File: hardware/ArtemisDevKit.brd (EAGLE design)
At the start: 94 x 38.1 mm, 231 parts, among them J1 USB, J10 SMD, J11 SMD, J12 PTH, J14 PTH, J2 CORTEX_JTAG_DEBUG_MINIMUM_PTH, J22 PTH, J23 PTH, J24 PTH, J25 PTH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

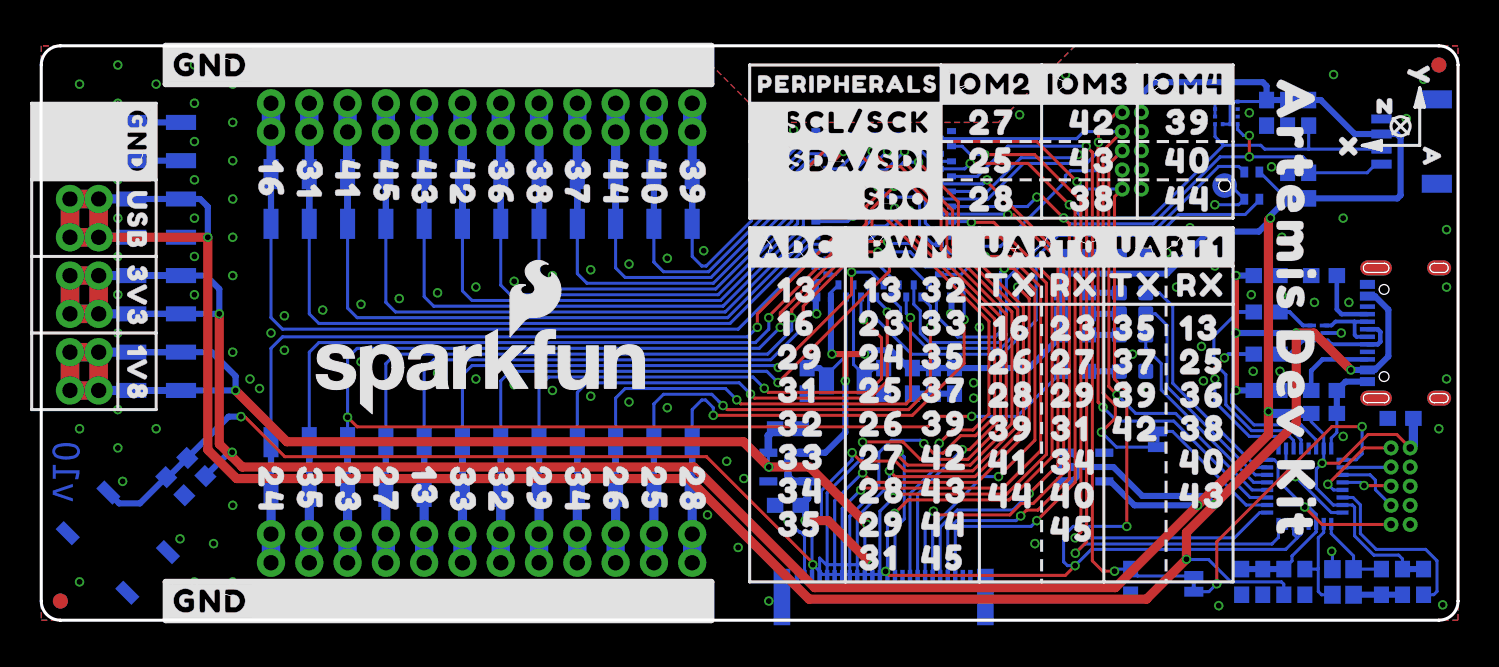
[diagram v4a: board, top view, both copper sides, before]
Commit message: add test points for interface JTAG
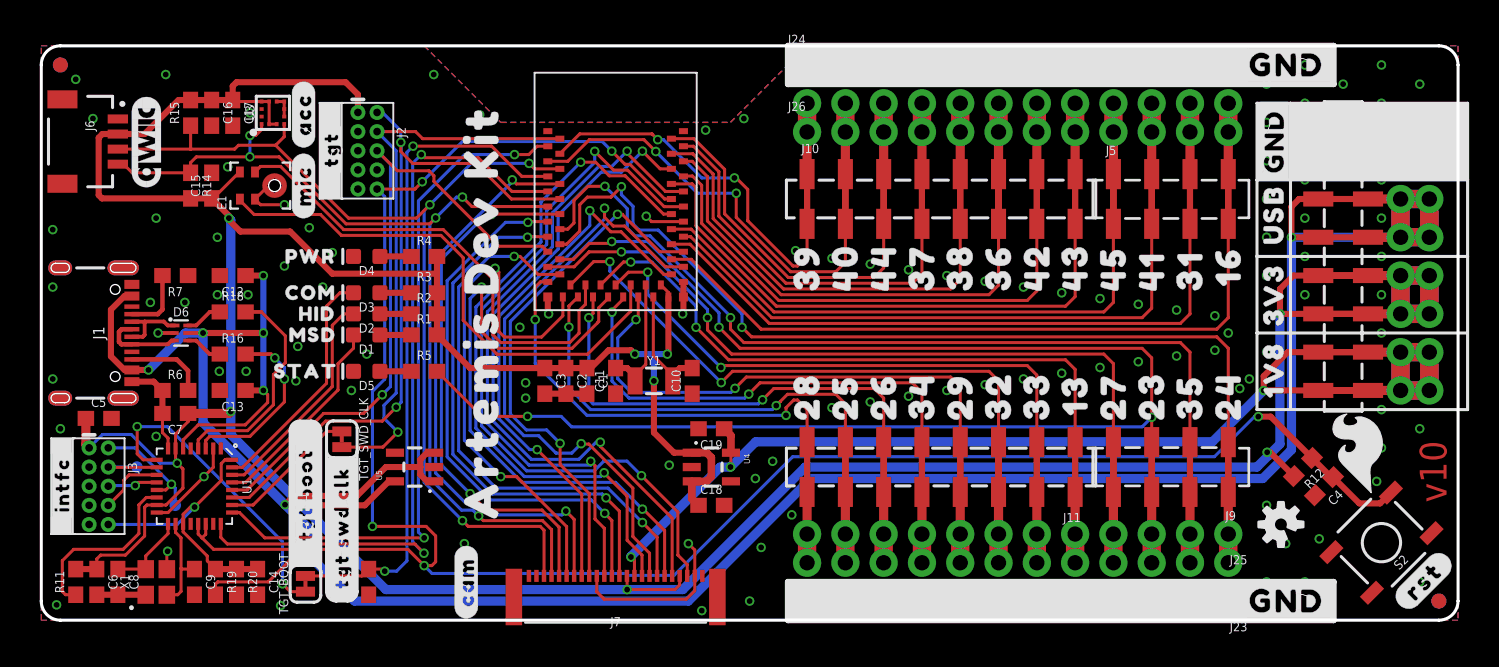
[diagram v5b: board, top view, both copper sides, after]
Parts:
- added TP1: INTFC_SWDIO, SparkFun-Connectors:PAD.03X.03
- added TP2: INTFC_SWDCLK, SparkFun-Connectors:PAD.03X.03
- moved FD1 91.4 mm to (1.27, 36.8), flipped to the top
- moved FD2 91.4 mm to (1.27, 36.8), flipped to the bottom
- moved FD3 91.4 mm to (92.7, 1.27), flipped to the top
- moved FD4 91.4 mm to (92.7, 1.27), flipped to the bottom
- moved U$135 91.2 mm to (1.40, 6.48), flipped to the top
- moved U$113 90.5 mm to (1.75, 30.7), flipped to the bottom
- moved J8 90.2 mm to (92.1, 33.0), flipped to the top
- moved U$115 89.5 mm to (2.22, 36.1), flipped to the bottom
- moved R11 89.4 mm to (2.29, 2.54), flipped to the top
- moved C6 86.6 mm to (3.68, 2.54), flipped to the top
- moved C5 86.4 mm to (3.81, 13.4), flipped to the top
- moved J12 86.4 mm to (90.2, 33.0), flipped to the top
- moved J3 86.4 mm to (3.81, 8.89), flipped to the top
- moved U$142 86.2 mm to (90.1, 1.02), flipped to the top
- moved C8 83.8 mm to (5.08, 2.54), flipped to the top
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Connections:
- net INTFC_SWDCLK: now also TP2.P$1
- net INTFC_SWDIO: now also TP1.P$1
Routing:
- net 3.3V: track 284.5 -> 277.1 mm, vias 11 -> 10
- net GND: track 113.0 -> 120.2 mm, vias 110 -> 112
- net INTFC_SWDCLK: track 3.22 -> 5.13 mm
- net CAMERA_VSYNC: track 44.0 -> 42.3 mm
- net CAMERA_D0: track 45.2 -> 43.6 mm
- net CAMERA_D1: track 50.7 -> 49.1 mm
- net INTFC_SWDIO: track 6.32 -> 7.82 mm
- net CAMERA_D3: track 46.1 -> 44.7 mm
- net 1.8V: track 89.3 -> 88.2 mm
- net CAMERA_TRIG: track 38.1 -> 37.0 mm
- net CAMERA_MCLK: track 42.1 -> 41.0 mm
- net !TGT_RST: track 141.8 -> 141.5 mm, vias 7 -> 5

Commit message: fix camera connector
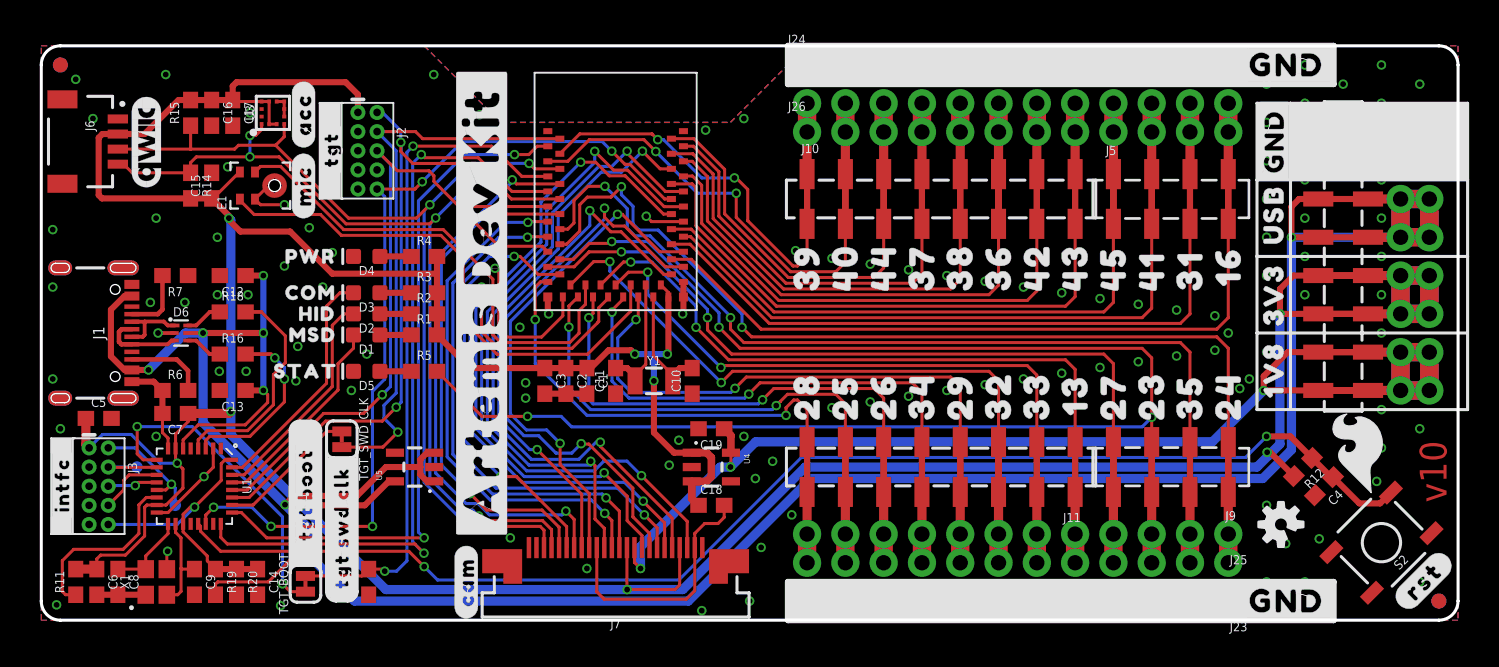
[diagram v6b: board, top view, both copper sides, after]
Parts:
- removed U$35: (no value), buzzard_labels:ARTEMIS_DEV_KIT0
- added U$122: (no value), buzzard_labels:#ARTEMIS_DEV_KIT#1
- J7: value CAMERA-HIMAX -> CAMERA-HIMAXBOTTOM-CONTACT; device SparkFun-Connectors:FPC05024-42201 -> SparkFun-Connectors:FPC-24-AMPHENOL-SFV24R-1STE1HLF
- U$36: device buzzard_labels:ARTEMIS_DEV_KIT1 -> buzzard_labels:#ARTEMIS_DEV_KIT#0
- moved U$36 37.4 mm to (11.2, 37.8), flipped to the bottom, turned to 270 degrees
- moved J7 0.13 mm to (38.1, 2.41)
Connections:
- new net !RST!_BTN: C4.1, R12.1, S2.3, U1.21
- net !TGT_RST: no longer C4.1, R12.1, S2.3, U1.21
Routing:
- net !RST!_BTN: track 0.00 -> 87.1 mm, vias 0 -> 2
- net !TGT_RST: track 141.5 -> 57.7 mm
- net GND: track 120.2 -> 125.7 mm, vias 112 -> 114
- net 3.3V: track 277.1 -> 280.8 mm
- net SCL: track 65.1 -> 63.3 mm
- net CAMERA_INT: track 39.2 -> 37.4 mm
- net CAMERA_D6: track 35.6 -> 33.7 mm
- net CAMERA_D2: track 45.8 -> 43.9 mm
- net CAMERA_D0: track 43.6 -> 41.7 mm
- net CAMERA_PCLK: track 36.5 -> 34.6 mm
- net CAMERA_MCLK: track 41.0 -> 39.2 mm
- net CAMERA_HSYNC: track 35.3 -> 33.4 mm
- net CAMERA_D7: track 36.3 -> 34.5 mm
- net CAMERA_D5: track 35.5 -> 33.6 mm
- net CAMERA_D4: track 35.8 -> 34.0 mm
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
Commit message: final design checklist
-removed I2C PU resistors
- switched bubble labels to UPPER CASE
- ran checklist
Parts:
- removed R14, R15: 2.2k, SparkFun-Resistors:0603
- removed U$133: (no value), buzzard_labels:4_#TGT_SWD_CLK#
- removed U$134: (no value), buzzard_labels:3_#TGT_BOOT#
- removed U$135: (no value), buzzard_labels:1_#INTFC#
- removed U$136: (no value), buzzard_labels:2_#TGT#
- removed U$139: (no value), buzzard_labels:12_#CAM#
- added U$123: (no value), buzzard_labels:#INTFC#2
- added U$124: (no value), buzzard_labels:#TGT_BOOT#4
- added U$125: (no value), buzzard_labels:#TGT_SWD_CLK#5
- added U$126: (no value), buzzard_labels:#CAM#13
- added U$35: (no value), buzzard_labels:#TGT#3
- U$137: device buzzard_labels:10_#MIC# -> buzzard_labels:#MIC#11
- U$138: device buzzard_labels:11_#ACC# -> buzzard_labels:#ACC#12
- U$142: device buzzard_labels:13_#RST# -> buzzard_labels:##RST##18
- moved U$122 1.27 mm to (29.2, 6.10)
- moved U$142 0.63 mm to (89.7, 0.56)
- moved U$138 0.38 mm to (17.4, 31.0)
- moved U$137 0.25 mm to (17.4, 26.4)
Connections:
- net 3.3V: no longer R14.2, R15.2
- net SCL: no longer R14.1
- net SDA: no longer R15.1
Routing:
- net SDA: track 65.3 -> 63.7 mm
- net SCL: track 63.3 -> 62.4 mm
- net CAMERA_D1: track 47.9 -> 47.3 mm
- net GND: vias 114 -> 116

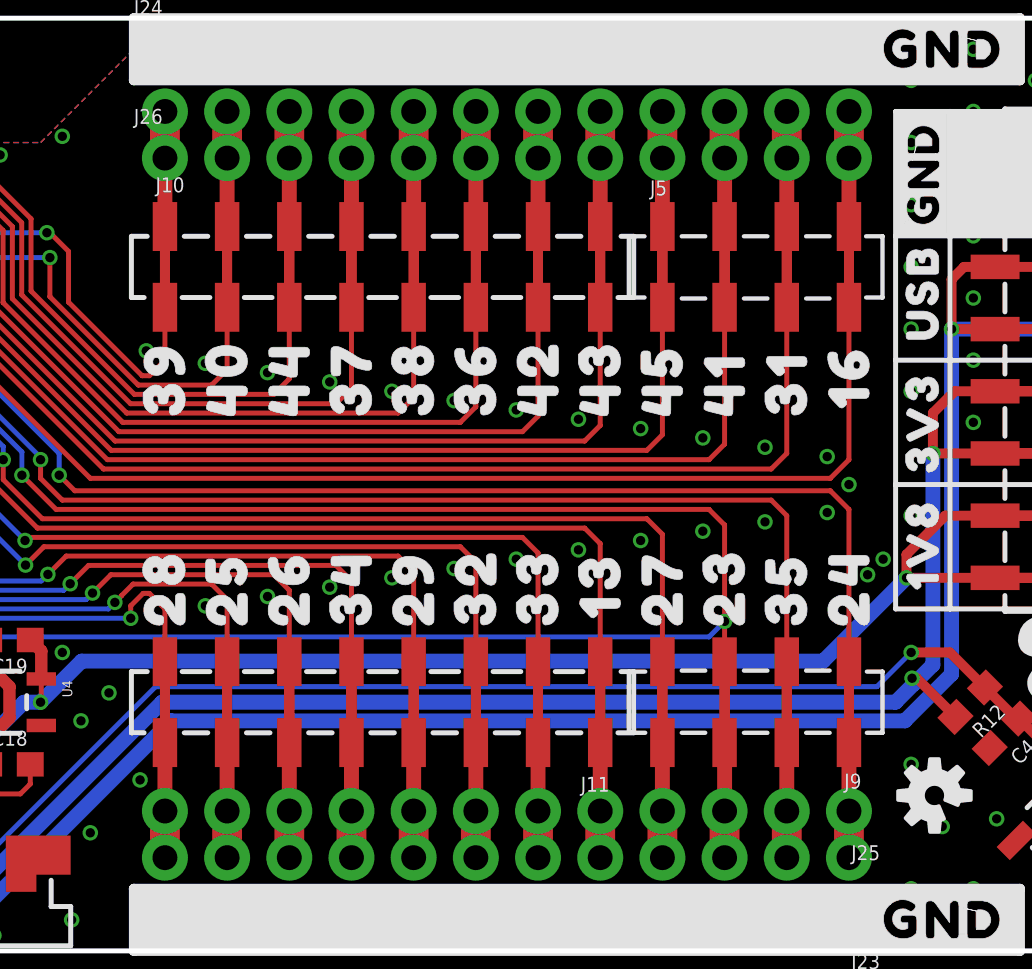
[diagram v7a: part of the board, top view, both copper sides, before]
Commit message: replace 8+4 smd headers with 12
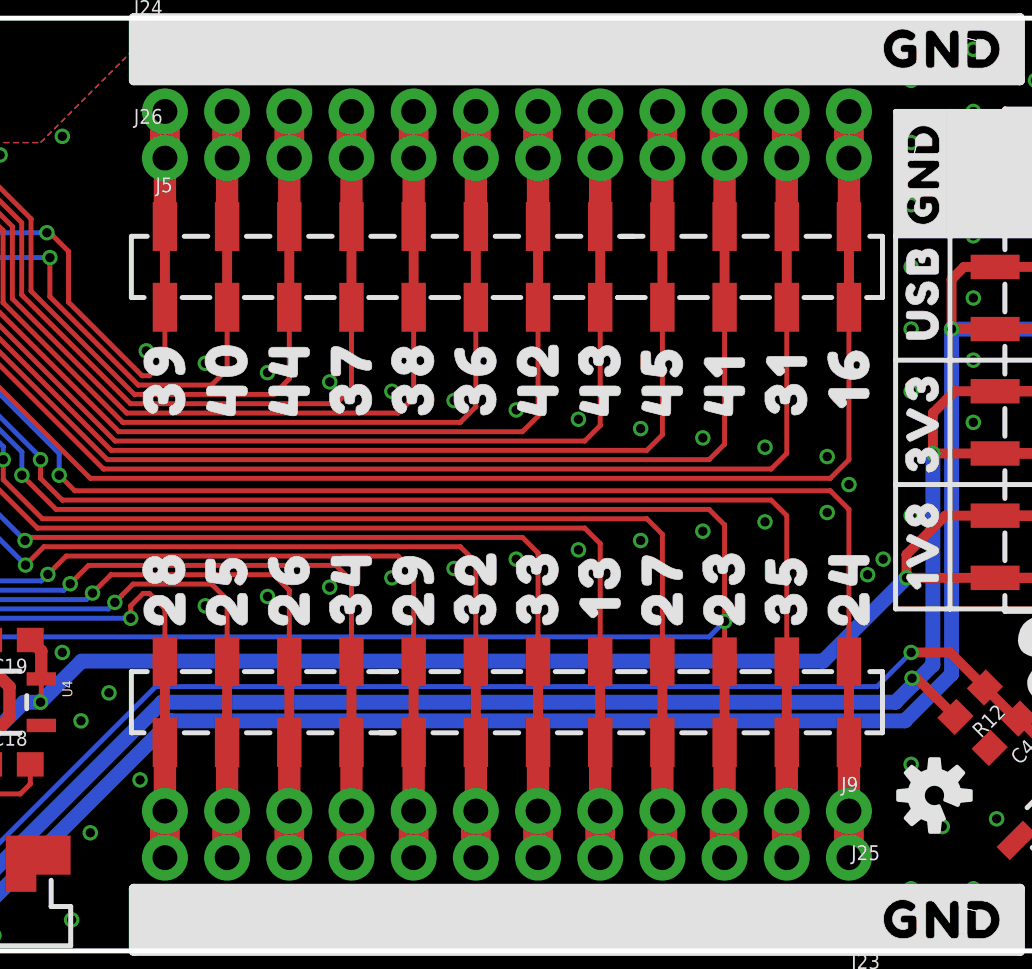
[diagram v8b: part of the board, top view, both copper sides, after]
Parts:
- removed J10, J11: SMD, SparkFun-Connectors:1X08_SMD_COMBINED
- J5, J9: value 1X04_SMD_STRAIGHT_COMBO -> (none); device SparkFun-Connectors:1X04_SMD_VERTICAL_COMBO -> SparkFun-Connectors:1X12_SMD_COMBINED
- moved J5 20.3 mm to (50.8, 27.9)
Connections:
- net D13: now also J9.5, J9.5@2; no longer J11.1, J11.1@2
- net D16: now also J5.12, J5.12@2; no longer J5.4, J5.4-2
- net D23_LED: now also J9.3@2; no longer J9.3-2
- net D24: now also J9.1@2; no longer J9.1-2
- net D25: now also J9.11, J9.11@2; no longer J11.7, J11.7@2
- net D26: now also J9.10, J9.10@2; no longer J11.6, J11.6@2
- net D27: now also J9.4@2; no longer J9.4-2
- net D28: now also J9.12, J9.12@2; no longer J11.8, J11.8@2
- net D29: now also J9.8, J9.8@2; no longer J11.4, J11.4@2
- net D31: now also J5.11, J5.11@2; no longer J5.3, J5.3-2
- net D32: now also J9.7, J9.7@2; no longer J11.3, J11.3@2
- net D33: now also J9.6, J9.6@2; no longer J11.2, J11.2@2
- net D34: now also J9.9, J9.9@2; no longer J11.5, J11.5@2
- net D35: now also J9.2@2; no longer J9.2-2
- net D36: now also J5.6, J5.6@2; no longer J10.6, J10.6@2
- net D37: now also J5.4, J5.4@2; no longer J10.4, J10.4@2
- net D38: now also J5.5, J5.5@2; no longer J10.5, J10.5@2
- net D39: now also J5.1, J5.1@2; no longer J10.1, J10.1@2
- net D40: now also J5.2, J5.2@2; no longer J10.2, J10.2@2
- net D41: now also J5.10, J5.10@2; no longer J5.2, J5.2-2
- net D42: now also J5.7, J5.7@2; no longer J10.7, J10.7@2
- net D43: now also J5.8, J5.8@2; no longer J10.8, J10.8@2
- net D44: now also J5.3, J5.3@2; no longer J10.3, J10.3@2
- net D45: now also J5.9, J5.9@2; no longer J5.1, J5.1-2
